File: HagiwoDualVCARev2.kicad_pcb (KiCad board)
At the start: 2 copper layers, 86 x 128.5 mm, 60 parts, among them J1 CV 1, J2 CV 2, J3 IN 1, J4 IN 2, J5 OUT 1, J6 OUT 2, U1 V2164M, U2 TL074

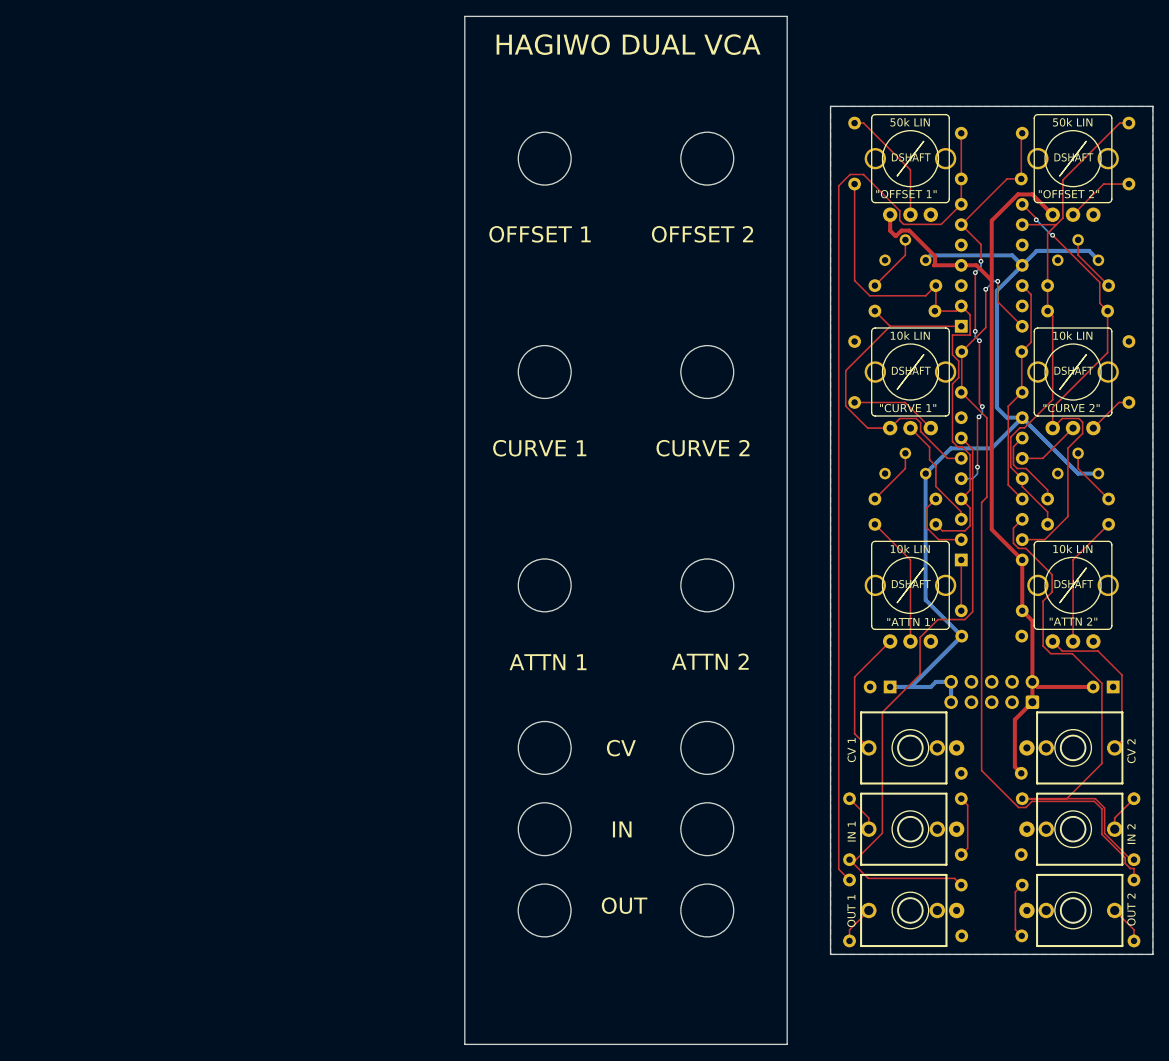
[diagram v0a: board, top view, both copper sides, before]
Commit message: fixed decoupling cap polarity issue, trimmer pot had wrong footprint, finalised silkscreening, etc
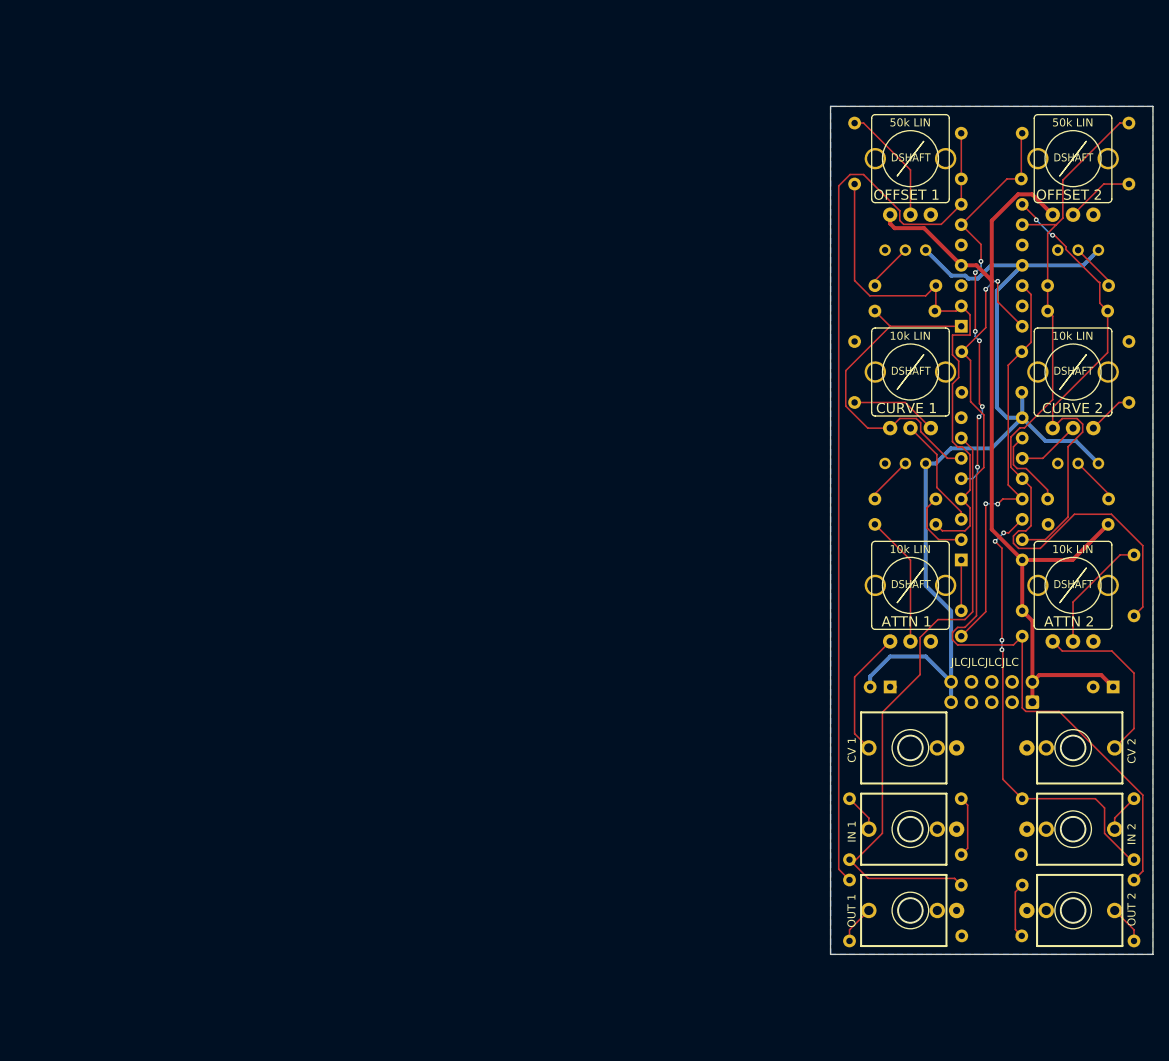
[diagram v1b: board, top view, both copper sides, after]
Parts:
- removed REF** (x6): GND, Library:Faceplate_Hole_Jack_3.5mm_NPTH
- removed REF** (x6): Faceplate_Hole_Pot_9mm_NPTH, Library:Faceplate_Hole_Pot_9mm_NPTH
- PWR1: footprint Library:IDC-Header_2x05_P2.54mm_Vertical_Euro_Power_Striped -> Library:IDC-Header_2x05_P2.54mm_Vertical_Euro_Power_Striped_ThickerText
- RV3: value 100k LIN 1 -> 100k LIN 1▼; footprint Potentiometer_THT:Potentiometer_Bourns_3296Y_Vertical -> Potentiometer_THT:Potentiometer_Bourns_3296W_Vertical
- RV4: value 10K LIN 1 -> 10K LIN 1▲; footprint Potentiometer_THT:Potentiometer_Bourns_3296Y_Vertical -> Potentiometer_THT:Potentiometer_Bourns_3296W_Vertical
- RV7: value 100k LIN 2 -> 100k LIN 2▼; footprint Potentiometer_THT:Potentiometer_Bourns_3296Y_Vertical -> Potentiometer_THT:Potentiometer_Bourns_3296W_Vertical
- RV8: value 10K LIN 2 -> 10K LIN 2▲; footprint Potentiometer_THT:Potentiometer_Bourns_3296Y_Vertical -> Potentiometer_THT:Potentiometer_Bourns_3296W_Vertical
- moved C9 33.0 mm to (179.8, 94.0)
- moved R16 31.4 mm to (168.9, 108.0), turned to 0 degrees
- moved C10 31.4 mm to (176.5, 77.5), turned to 180 degrees
- moved R5 4.96 mm to (190.5, 97.8), turned to -90 degrees
- moved RV3 1.27 mm to (164.5, 59.7)
- moved RV4 1.27 mm to (164.5, 86.4)
- moved RV7 1.27 mm to (186.1, 59.7)
- moved RV8 1.27 mm to (186.1, 86.4)
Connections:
- C7 pad 1: GND -> +12V
- C7 pad 2: +12V -> GND
- C8 pad 1: -12V -> GND
- C8 pad 2: GND -> -12V
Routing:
- net Net-(U2C--): track 64.0 -> 96.0 mm
- net Net-(U2D-+): track 29.1 -> 51.7 mm, vias 0 -> 2
- net Net-(R12-Pad2): track 69.4 -> 57.1 mm, vias 0 -> 4
- net Net-(C6-Pad2): track 100.3 -> 106.2 mm
- net +12V: track 109.0 -> 112.7 mm
- net -12V: track 119.2 -> 122.4 mm
- net Net-(J2-SIG): track 19.9 -> 22.1 mm
- net Net-(R5-Pad1): track 16.5 -> 15.0 mm
- net Net-(R7-Pad1): track 7.29 -> 6.02 mm
- net Net-(R3-Pad1): track 7.29 -> 6.02 mm
- net Net-(R8-Pad1): track 7.29 -> 6.02 mm
- net Net-(R4-Pad1): track 7.29 -> 6.02 mm
- net GND: track 0.00 -> 0.63 mm
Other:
- board size 86 x 128.5 mm -> 40.3 x 106 mm
- board text added: "-HAGIWO DUAL VCA REV 2-"
- board text added: "JLCJLCJLCJLC"
- board text added: "PCB BY 42 BERLIN SYNTHLAB"
- board text added: "V1.0"
- board text added: "https://github.com/fablabnk/SynthLabProjects"
- board text removed: "ATTN 1"
- board text removed: "ATTN 2"
- board text removed: "CURVE 1"
- board text removed: "CURVE 2"
- board text removed: "CV"
- board text removed: "HAGIWO DUAL VCA"
- board text removed: "IN"
- board text removed: "OFFSET 1"
- board text removed: "OFFSET 2"
- board text removed: "OUT"
- board text removed: "{dblquote}ATTN 1{dblquote}"
- board text removed: "{dblquote}ATTN 2{dblquote}"
- board text removed: "{dblquote}CURVE 1{dblquote}"
- board text removed: "{dblquote}CURVE 2{dblquote}"
- board text removed: "{dblquote}OFFSET 1{dblquote}"
- board text removed: "{dblquote}OFFSET 2{dblquote}"

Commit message: ready for production
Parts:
- added C11: 1uF, Capacitor_THT:C_Axial_L3.8mm_D2.6mm_P7.50mm_Horizontal, B.Cu at (56.5, 73.2)
- added C12: 1uF, Capacitor_THT:C_Axial_L3.8mm_D2.6mm_P7.50mm_Horizontal, B.Cu at (77.9, 73.2)
- C1, C2, C5, C6: value 101 -> 100pF
- C10, C9: value 105 -> 1uF
- C3, C4: value 471 -> 470pF
- RV3: value 100k LIN 1▼ -> 100k LIN 1
- RV4: value 10K LIN 1▲ -> 10K LIN 1
- RV7: value 100k LIN 2▼ -> 100k LIN 2
- RV8: value 10K LIN 2▲ -> 10K LIN 2
- moved R3 104.7 mm to (53.4, 65.6), turned to -90 degrees
- moved C7 104.6 mm to (83.7, 123.4), turned to 0 degrees
- moved C8 104.4 mm to (56.0, 123.4), turned to 0 degrees
- moved R11 103.3 mm to (53.0, 145.0), turned to 90 degrees
- moved R5 103.1 mm to (88.7, 114.5), turned to 90 degrees
- moved R9 102.6 mm to (53.4, 80.2)
- moved R2 102.6 mm to (53.4, 52.9)
- moved R17 102.3 mm to (53.0, 147.5)
- moved C2 102.3 mm to (77.9, 76.6)
- moved C6 102.2 mm to (74.7, 81.5)
- moved C3 102.2 mm to (67.2, 154.5)
- moved J1 102.2 mm to (60.8, 131.0)
- moved J3 102.2 mm to (60.8, 141.2)
- moved J5 102.2 mm to (60.8, 151.3)
- moved PWR1 102.2 mm to (76.0, 125.3)
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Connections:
- C6 pad 1: Net-(U2D-+) -> Net-(U2D--)
- R16 pad 1: Net-(U2D-+) -> Net-(U2D--)
- U1 pad 13: Net-(U2D-+) -> Net-(U2D--)
- U1 pad 14: Net-(R12-Pad2) -> Net-(C2-Pad2)
- U1 pad 15: Net-(C2-Pad2) -> Net-(R12-Pad2)
- U2 pad 12: Net-(U2D-+) -> GND
- U2 pad 13: GND -> Net-(U2D--)
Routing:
- net Net-(C11-Pad1): track 0.00 -> 78.3 mm
- net Net-(U2D-+): track 51.7 -> 0.00 mm, vias 2 -> 0
- net Net-(U2D--): track 0.00 -> 49.5 mm, vias 0 -> 2
- net Net-(C6-Pad2): track 106.2 -> 95.7 mm
- net Net-(U2C--): track 96.0 -> 106.1 mm, vias 0 -> 3
- net Net-(U2A--): track 68.1 -> 75.5 mm, vias 0 -> 1
- net Net-(R11-Pad2): track 77.4 -> 71.2 mm
- net Net-(R5-Pad1): track 15.0 -> 8.95 mm
- net Net-(J2-SIG): track 22.1 -> 16.5 mm
- net Net-(R12-Pad2): track 57.1 -> 52.6 mm, vias 4 -> 2
- net Net-(C2-Pad2): track 59.3 -> 54.9 mm, vias 2 -> 0
- net +12V: track 112.7 -> 108.7 mm
- net Net-(U2B--): track 51.0 -> 54.8 mm, vias 7 -> 1
- net Net-(C1-Pad2): track 42.6 -> 46.3 mm
- net Net-(R4-Pad2): track 8.96 -> 6.40 mm
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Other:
- board text added: "HAGIWO DUAL VCA REV 2"
- board text added: "SynthLab"
- board text removed: "-HAGIWO DUAL VCA REV 2-"

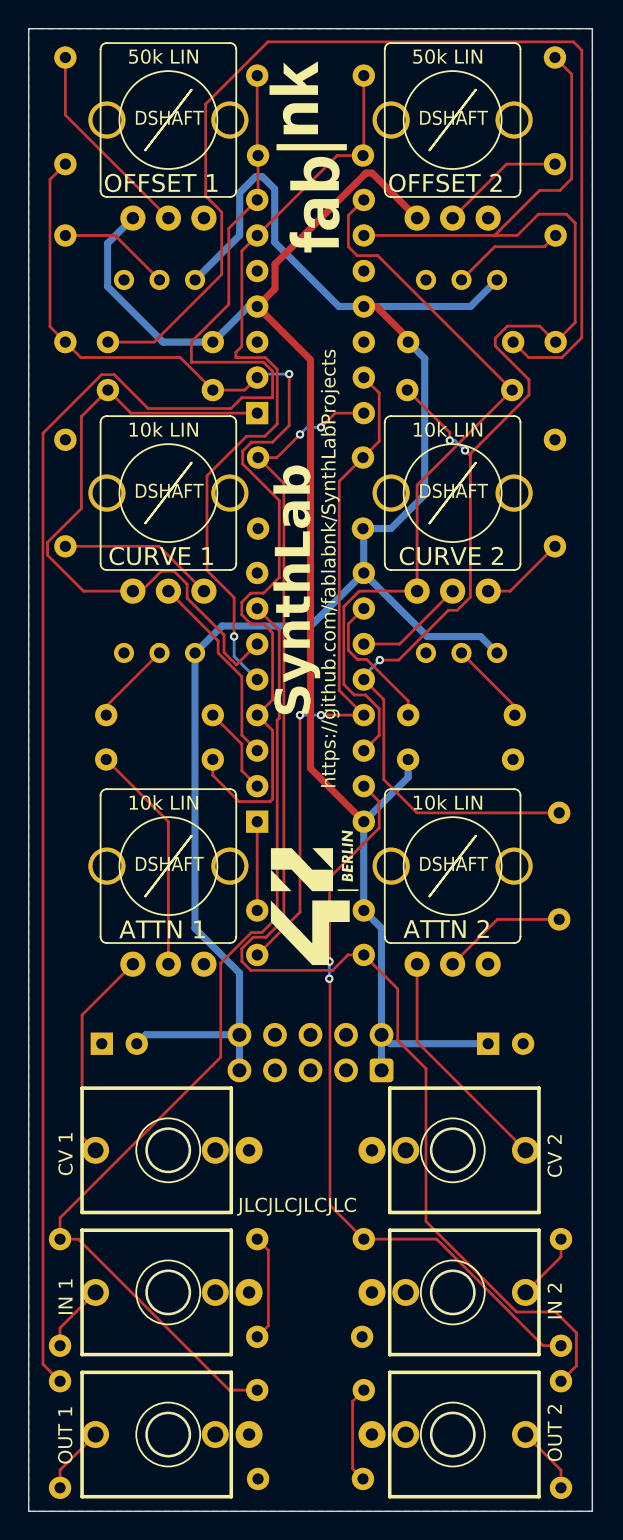
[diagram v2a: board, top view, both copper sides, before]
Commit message: v1.0 ready for production - added outline of full HP board size on User.Drawings layer
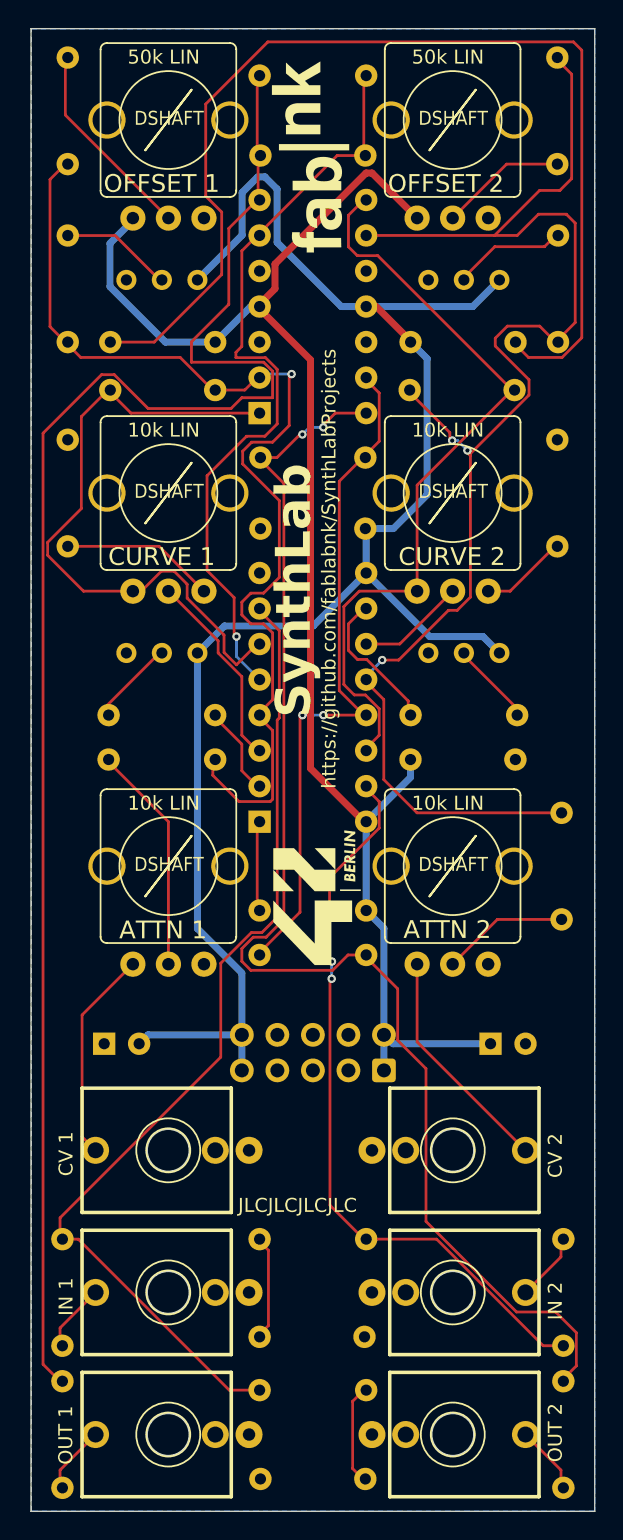
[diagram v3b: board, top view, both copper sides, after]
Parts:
- R19: value 7.5K -> 7.5k
- moved C1 0.17 mm to (64.1, 76.6)
- moved C10 0.17 mm to (74.9, 86.5)
- moved C11 0.17 mm to (56.6, 73.2)
- moved C12 0.17 mm to (78.1, 73.2)
- moved C2 0.17 mm to (78.0, 76.6)
- moved C3 0.17 mm to (67.4, 154.5)
- moved C4 0.17 mm to (74.8, 144.3)
- moved C5 0.17 mm to (74.9, 59.9)
- moved C6 0.17 mm to (74.9, 81.5)
- moved C9 0.17 mm to (85.6, 103.1)
- moved PWR1 0.17 mm to (76.2, 125.3)
- moved R1 0.17 mm to (56.5, 103.0)
- moved R10 0.17 mm to (88.6, 80.2)
- moved R11 0.17 mm to (53.2, 145.0)
- moved R12 0.17 mm to (89.0, 137.3)
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
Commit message: v1.1 ready for check
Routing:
- net Net-(C11-Pad1): track 78.3 -> 58.4 mm, vias 0 -> 4
- net Net-(RV10-Pad2): track 7.92 -> 27.1 mm
- net Net-(R12-Pad2): track 52.6 -> 68.6 mm
- net Net-(C2-Pad2): track 54.9 -> 70.8 mm
- net Net-(C5-Pad2): track 118.2 -> 102.4 mm, vias 0 -> 8
- net Net-(R11-Pad2): track 71.2 -> 85.1 mm
- net Net-(U2A--): track 75.5 -> 62.9 mm, vias 1 -> 3
- net -12V: track 122.8 -> 134.9 mm
- net Net-(U2B--): track 54.8 -> 64.6 mm, vias 1 -> 7
- net Net-(U2C--): track 106.1 -> 97.4 mm, vias 3 -> 2
- net Net-(C1-Pad2): track 46.3 -> 41.6 mm
- net Net-(RV9-Pad2): track 14.0 -> 17.8 mm
- net Net-(C6-Pad2): track 95.7 -> 99.3 mm, vias 2 -> 0
- net Net-(R4-Pad2): track 6.40 -> 9.26 mm
- net +12V: track 108.7 -> 111.3 mm
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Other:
- board text added: "V1.1"
- board text removed: "V1.0"

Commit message: updating wwith Dmitri's corrections
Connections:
- RV1 pad 1: Net-(J1-SIG) -> GND
- RV1 pad 3: GND -> Net-(J1-SIG)
- RV10 pad 1: Net-(C2-Pad2) -> Net-(R10-Pad2)
- RV10 pad 3: Net-(R10-Pad2) -> Net-(C2-Pad2)
- RV2 pad 1: +12V -> unconnected-(RV2-Pad1)
- RV2 pad 3: unconnected-(RV2-Pad3) -> +12V
- RV5 pad 1: Net-(J2-SIG) -> GND
- RV5 pad 3: GND -> Net-(J2-SIG)
- RV6 pad 1: +12V -> unconnected-(RV6-Pad1)
- RV6 pad 3: unconnected-(RV6-Pad3) -> +12V
- RV9 pad 1: Net-(C1-Pad2) -> Net-(R9-Pad2)
- RV9 pad 3: Net-(R9-Pad2) -> Net-(C1-Pad2)
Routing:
- net Net-(C1-Pad2): track 41.6 -> 34.1 mm
- net Net-(R10-Pad2): track 6.27 -> 11.4 mm
- net Net-(J1-SIG): track 15.2 -> 20.3 mm
- net Net-(R9-Pad2): track 11.1 -> 6.65 mm
- net +12V: track 111.3 -> 113.1 mm
- net Net-(J2-SIG): track 16.5 -> 15.8 mm
- net Net-(C2-Pad2): track 70.8 -> 70.4 mm, vias 0 -> 1
